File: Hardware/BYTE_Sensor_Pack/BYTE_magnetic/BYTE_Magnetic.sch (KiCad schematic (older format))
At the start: 18 parts, among them J1 PCB, M1 Motor_DC, U1 SI7210-B-11-IM2, U2 DRV2605YZFR, U3 Si7217-B-01-IV, U4 SI7210-B-12-IM2, U5 SI7210-B-13-IM2, U6 SI7210-B-14-IM2

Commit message: update sch magnetic
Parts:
- gave numbers to parts that had none: 4
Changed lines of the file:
@@
 	3385 3925 3385 3990
 $Comp
-L power:+3.3V #PWR?
+L power:+3.3V #PWR0122
 U 1 1 613FDA44
 P 3385 3685
-F 0 "#PWR?" H 3385 3535 50  0001 C CNN
+F 0 "#PWR0122" H 3385 3535 50  0001 C CNN
 F 1 "+3.3V" H 3400 3858 50  0000 C CNN
 F 2 "" H 3385 3685 50  0001 C CNN
@@
 $EndComp
 $Comp
-L Device:C_Small C?
+L Device:C_Small C2
 U 1 1 613FDA4E
 P 3385 3825
-F 0 "C?" H 3477 3871 50  0000 L CNN
+F 0 "C2" H 3477 3871 50  0000 L CNN
 F 1 "0.1uF" H 3477 3780 50  0000 L CNN
 F 2 "Capacitor_SMD:C_0603_1608Metric" H 3385 3825 50  0001 C CNN
@@
 $EndComp
 $Comp
-L power:GND #PWR?
+L power:GND #PWR0123
 U 1 1 613FDA58
 P 3385 3990
-F 0 "#PWR?" H 3385 3740 50  0001 C CNN
+F 0 "#PWR0123" H 3385 3740 50  0001 C CNN
 F 1 "GND" H 3390 3817 50  0000 C CNN
 F 2 "" H 3385 3990 50  0001 C CNN
@@
 	5150 3925 5150 3990
 $Comp
-L power:+3.3V #PWR?
+L power:+3.3V #PWR0124
 U 1 1 6140C4E9
 P 5150 3685
-F 0 "#PWR?" H 5150 3535 50  0001 C CNN
+F 0 "#PWR0124" H 5150 3535 50  0001 C CNN
 F 1 "+3.3V" H 5165 3858 50  0000 C CNN
 F 2 "" H 5150 3685 50  0001 C CNN
@@
 $EndComp
 $Comp
-L Device:C_Small C?
+L Device:C_Small C3
 U 1 1 6140C4F3
 P 5150 3825
-F 0 "C?" H 5242 3871 50  0000 L CNN
+F 0 "C3" H 5242 3871 50  0000 L CNN
 F 1 "0.1uF" H 5242 3780 50  0000 L CNN
 F 2 "Capacitor_SMD:C_0603_1608Metric" H 5150 3825 50  0001 C CNN
@@
 $EndComp
 $Comp
-L power:GND #PWR?
+L power:GND #PWR0125
 U 1 1 6140C4FD
 P 5150 3990
-F 0 "#PWR?" H 5150 3740 50  0001 C CNN
+F 0 "#PWR0125" H 5150 3740 50  0001 C CNN
 F 1 "GND" H 5155 3817 50  0000 C CNN
 F 2 "" H 5150 3990 50  0001 C CNN
@@
 	7130 3870 7130 3935
 $Comp
-L power:+3.3V #PWR?
+L power:+3.3V #PWR0126
 U 1 1 614205AE
 P 7130 3630
-F 0 "#PWR?" H 7130 3480 50  0001 C CNN
+F 0 "#PWR0126" H 7130 3480 50  0001 C CNN
 F 1 "+3.3V" H 7145 3803 50  0000 C CNN
 F 2 "" H 7130 3630 50  0001 C CNN
@@
 $EndComp
 $Comp
-L Device:C_Small C?
+L Device:C_Small C6
 U 1 1 614205B8
 P 7130 3770
-F 0 "C?" H 7222 3816 50  0000 L CNN
+F 0 "C6" H 7222 3816 50  0000 L CNN
 F 1 "0.1uF" H 7222 3725 50  0000 L CNN
 F 2 "Capacitor_SMD:C_0603_1608Metric" H 7130 3770 50  0001 C CNN
@@
 $EndComp
 $Comp
-L power:GND #PWR?
+L power:GND #PWR0127
 U 1 1 614205C2
 P 7130 3935
-F 0 "#PWR?" H 7130 3685 50  0001 C CNN
+F 0 "#PWR0127" H 7130 3685 50  0001 C CNN
 F 1 "GND" H 7135 3762 50  0000 C CNN
 F 2 "" H 7130 3935 50  0001 C CNN
@@
 	8955 3925 8955 3990
 $Comp
-L power:+3.3V #PWR?
+L power:+3.3V #PWR0128
 U 1 1 61428F42
 P 8955 3685
-F 0 "#PWR?" H 8955 3535 50  0001 C CNN
+F 0 "#PWR0128" H 8955 3535 50  0001 C CNN
 F 1 "+3.3V" H 8970 3858 50  0000 C CNN
 F 2 "" H 8955 3685 50  0001 C CNN
@@
 $EndComp
 $Comp
-L Device:C_Small C?
+L Device:C_Small C7
 U 1 1 61428F4C
 P 8955 3825
-F 0 "C?" H 9047 3871 50  0000 L CNN
+F 0 "C7" H 9047 3871 50  0000 L CNN
 F 1 "0.1uF" H 9047 3780 50  0000 L CNN
 F 2 "Capacitor_SMD:C_0603_1608Metric" H 8955 3825 50  0001 C CNN
@@
 $EndComp
 $Comp
-L power:GND #PWR?
+L power:GND #PWR0129
 U 1 1 61428F56
 P 8955 3990
-F 0 "#PWR?" H 8955 3740 50  0001 C CNN
+F 0 "#PWR0129" H 8955 3740 50  0001 C CNN
 F 1 "GND" H 8960 3817 50  0000 C CNN
 F 2 "" H 8955 3990 50  0001 C CNN

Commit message: update magnetic layout
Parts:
- removed C1, C2: 0.1uF, Capacitor_SMD:C_0603_1608Metric, symbol Device:C_Small
- removed J1: PCB, BYTE_Sensors:Magnetic_PCB, symbol Connector_Generic:Conn_01x06
- removed R3: 2.2K, Resistor_SMD:R_0603_1608Metric, symbol Device:R_Small
- removed U1: SI7210-B-11-IM2, BYTE_Sensors:SON40P140X160X40-8N-D, symbol magnetic_sensor:SI7210-B-10-IM2
- removed U2: DRV2605YZFR, BYTE_Sensors:BGA9C50P3X3_144X144X62, symbol BYTE_Magnetic-rescue:DRV2605YZFR-capacitive_sensor
- removed U3: Si7217-B-01-IV, BYTE_Sensors:SOT95P275X125-5N, symbol magnetic_sensor:Si7217-B-01-IV
- added J1: Input, BYTE_Sensors:Flex_Connector, symbol Connector_Generic:Conn_01x05
- added U1: DRV2605LDGS, Package_SO:VSSOP-10_3x3mm_P0.5mm, symbol Driver_Haptic:DRV2605LDGS
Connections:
- net labels removed: ADD0, ADD1, INT, OUT2, REG, SLEEP
- wire segments 63 -> 53
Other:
- note removed: "ADDR = 0x30"
- note removed: "Low(Open-drain)"
- moved on the sheet: C4, M1

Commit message: update magnetic sensor, merge with FSR
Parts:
- added C1: 1uF, Capacitor_SMD:C_0603_1608Metric, symbol Device:C_Small
- added J2: FSR, BYTE_Sensors:FSR_13mm, symbol Connector_Generic:Conn_01x04
- added R3, R4, R5, R6: 10K, Resistor_SMD:R_0603_1608Metric, symbol Device:R_Small
- added U2: ADS1115IDGS, Package_SO:TSSOP-10_3x3mm_P0.5mm, symbol Analog_ADC:ADS1115IDGS
- M1: footprint (none) -> BYTE_Sensors:VLV041235L
- U4, U5, U6: symbol magnetic_sensor:SI7210-B-10-IM2 -> BYTE_Magnetic-rescue:SI7210-B-10-IM2-magnetic_sensor
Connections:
- net labels added: A0, A1, A2, A3
- wire segments 53 -> 81
- no-connect marks 3 -> 1

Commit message: update pcbs
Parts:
- removed R1, R2: 2.2K, Resistor_SMD:R_0603_1608Metric, symbol Device:R_Small
- removed R3, R4, R5, R6: 10K, Resistor_SMD:R_0603_1608Metric, symbol Device:R_Small
- added RN1: R_Pack04, Resistor_SMD:R_Array_Convex_4x0603, symbol Device:R_Pack04
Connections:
- net A0: now also RN1.3 (R3.1)
- net A1: now also RN1.4 (R4.1)
- net A2: now also RN1.1 (R1.1)
- net A3: now also RN1.2 (R2.1)
- net GND: now also RN1.5 (R4.2), RN1.6 (R3.2), RN1.7 (R2.2), RN1.8 (R1.2)
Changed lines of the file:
@@
 Comment4 ""
 $EndDescr
-Text Label 2020 1260 0    50   ~ 0
-SCL
-Text Label 2020 1360 0    50   ~ 0
-SDA
-$Comp
-L power:+3.3V #PWR0107
-U 1 1 6139A81A
-P 2450 980
-F 0 "#PWR0107" H 2450 830 50  0001 C CNN
-F 1 "+3.3V" H 2465 1153 50  0000 C CNN
-F 2 "" H 2450 980 50  0001 C CNN
-F 3 "" H 2450 980 50  0001 C CNN
-	1    2450 980
-	1    0    0    -1
-$EndComp
-$Comp
-L power:+3.3V #PWR0108
-U 1 1 6139B3E0
-P 2725 975
-F 0 "#PWR0108" H 2725 825 50  0001 C CNN
-F 1 "+3.3V" H 2740 1148 50  0000 C CNN
-F 2 "" H 2725 975 50  0001 C CNN
-F 3 "" H 2725 975 50  0001 C CNN
-	1    2725 975
-	1    0    0    -1
-$EndComp
-$Comp
-L Device:R_Small R1
-U 1 1 6139B985
-P 2450 1115
-F 0 "R1" H 2315 1155 50  0000 L CNN
-F 1 "2.2K" H 2245 1070 50  0000 L CNN
-F 2 "Resistor_SMD:R_0603_1608Metric" H 2450 1115 50  0001 C CNN
-F 3 "~" H 2450 1115 50  0001 C CNN
-	1    2450 1115
-	1    0    0    -1
-$EndComp
-Wire Wire Line
-	2725 975  2725 1015
-Wire Wire Line
-	2450 980  2450 1015
-Wire Wire Line
-	2450 1260 2450 1215
-Wire Wire Line
-	2020 1260 2450 1260
-Wire Wire Line
-	2020 1360 2725 1360
-Wire Wire Line
-	2725 1215 2725 1360
-$Comp
-L Device:R_Small R2
-U 1 1 6139C2A7
-P 2725 1115
-F 0 "R2" H 2590 1150 50  0000 L CNN
-F 1 "2.2K" H 2515 1080 50  0000 L CNN
-F 2 "Resistor_SMD:R_0603_1608Metric" H 2725 1115 50  0001 C CNN
-F 3 "~" H 2725 1115 50  0001 C CNN
-	1    2725 1115
-	1    0    0    -1
-$EndComp
 Wire Wire Line
 	9475 1420 9985 1420
@@
 $EndComp
 $Comp
-L Device:R_Small R3
-U 1 1 6146D0E5
-P 4305 2635
-F 0 "R3" V 4300 2585 50  0000 L CNN
-F 1 "10K" V 4300 2195 50  0000 L CNN
-F 2 "Resistor_SMD:R_0603_1608Metric" H 4305 2635 50  0001 C CNN
-F 3 "~" H 4305 2635 50  0001 C CNN
-	1    4305 2635
+L Device:R_Pack04 RN1
+U 1 1 61491CB7
+P 4150 2600
+F 0 "RN1" H 4338 2646 50  0000 L CNN
+F 1 "R_Pack04" H 4338 2555 50  0000 L CNN
+F 2 "Resistor_SMD:R_Array_Convex_4x0603" V 4425 2600 50  0001 C CNN
+F 3 "~" H 4150 2600 50  0001 C CNN
+	1    4150 2600
 	-1   0    0    1
 $EndComp
-Text Label 4005 2355 3    50   ~ 0
+Wire Wire Line
+	4050 2800 4150 2800
+Wire Wire Line
+	4150 2800 4250 2800
+Connection ~ 4150 2800
+Wire Wire Line
+	4250 2800 4350 2800
+Connection ~ 4250 2800
+$Comp
+L power:GND #PWR0107
+U 1 1 614A2797
+P 4350 2850
+F 0 "#PWR0107" H 4350 2600 50  0001 C CNN
+F 1 "GND" H 4355 2677 50  0000 C CNN
+F 2 "" H 4350 2850 50  0001 C CNN
+F 3 "" H 4350 2850 50  0001 C CNN
+	1    4350 2850
+	1    0    0    -1
+$EndComp
+Wire Wire Line
+	4350 2850 4350 2800
+Connection ~ 4350 2800
+Wire Wire Line
+	4050 2250 4050 2400
+Wire Wire Line
+	4150 2400 4150 2250
+Wire Wire Line
+	4250 2400 4250 2250
+Wire Wire Line
+	4350 2400 4350 2250
+Text Label 4050 2250 3    50   ~ 0
+A1
+Text Label 4150 2250 3    50   ~ 0
 A0
-Wire Wire Line
-	4005 2355 4005 2535
-Text Label 4105 2355 3    50   ~ 0
-A1
-Wire Wire Line
-	4105 2355 4105 2535
-Text Label 4205 2355 3    50   ~ 0
+Text Label 4350 2250 3    50   ~ 0
 A2
-Wire Wire Line
-	4205 2355 4205 2535
-Text Label 4305 2355 3    50   ~ 0
+Text Label 4250 2250 3    50   ~ 0
 A3
-Wire Wire Line
-	4305 2355 4305 2535
-$Comp
-L Device:R_Small R4
-U 1 1 61479B09
-P 4205 2635
-F 0 "R4" V 4200 2580 50  0000 L CNN
-F 1 "10K" V 4205 2195 50  0000 L CNN
-F 2 "Resistor_SMD:R_0603_1608Metric" H 4205 2635 50  0001 C CNN
-F 3 "~" H 4205 2635 50  0001 C CNN
-	1    4205 2635
-	-1   0    0    1
-$EndComp
-$Comp
-L Device:R_Small R5
-U 1 1 6147E339
-P 4105 2635
-F 0 "R5" V 4100 2580 50  0000 L CNN
-F 1 "10K" V 4105 2200 50  0000 L CNN
-F 2 "Resistor_SMD:R_0603_1608Metric" H 4105 2635 50  0001 C CNN
-F 3 "~" H 4105 2635 50  0001 C CNN
-	1    4105 2635
-	-1   0    0    1
-$EndComp
-$Comp
-L Device:R_Small R6
-U 1 1 6147E7F5
-P 4005 2635
-F 0 "R6" V 4000 2580 50  0000 L CNN
-F 1 "10K" V 4005 2200 50  0000 L CNN
-F 2 "Resistor_SMD:R_0603_1608Metric" H 4005 2635 50  0001 C CNN
-F 3 "~" H 4005 2635 50  0001 C CNN
-	1    4005 2635
-	-1   0    0    1
-$EndComp
-Wire Wire Line
-	4005 2735 4005 2805
-Wire Wire Line
-	4005 2805 4105 2805
-Connection ~ 4305 2805
-Wire Wire Line
-	4305 2805 4305 2735
-Wire Wire Line
-	4205 2735 4205 2805
-Connection ~ 4205 2805
-Wire Wire Line
-	4205 2805 4305 2805
-Wire Wire Line
-	4105 2735 4105 2805
-Connection ~ 4105 2805
-Wire Wire Line
-	4105 2805 4205 2805
-$Comp
-L power:GND #PWR0118
-U 1 1 61495E33
-P 4305 2885
-F 0 "#PWR0118" H 4305 2635 50  0001 C CNN
-F 1 "GND" H 4310 2712 50  0000 C CNN
-F 2 "" H 4305 2885 50  0001 C CNN
-F 3 "" H 4305 2885 50  0001 C CNN
-	1    4305 2885
-	1    0    0    -1
-$EndComp
-Wire Wire Line
-	4305 2805 4305 2885
 $EndSCHEMATC

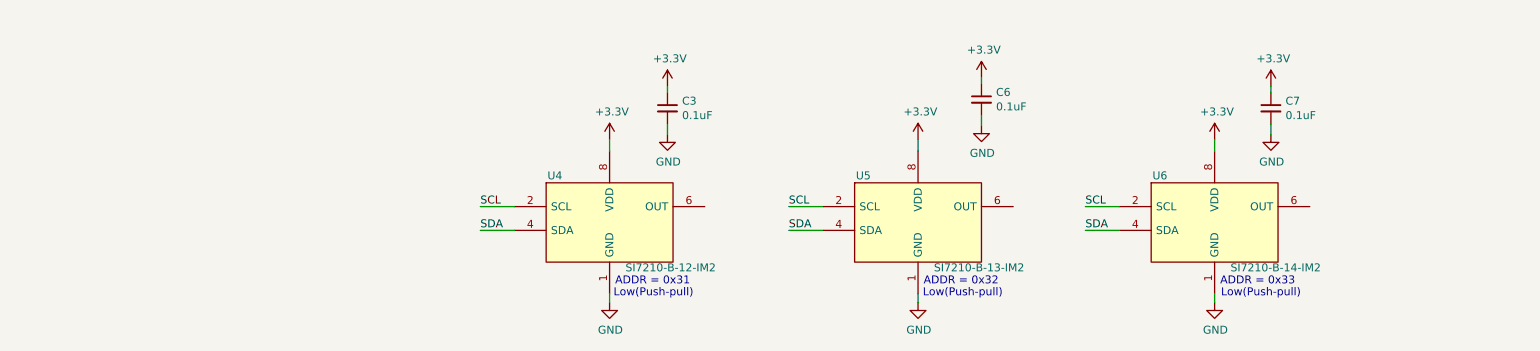
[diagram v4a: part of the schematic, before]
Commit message: update magentic adding I2C I/O controller
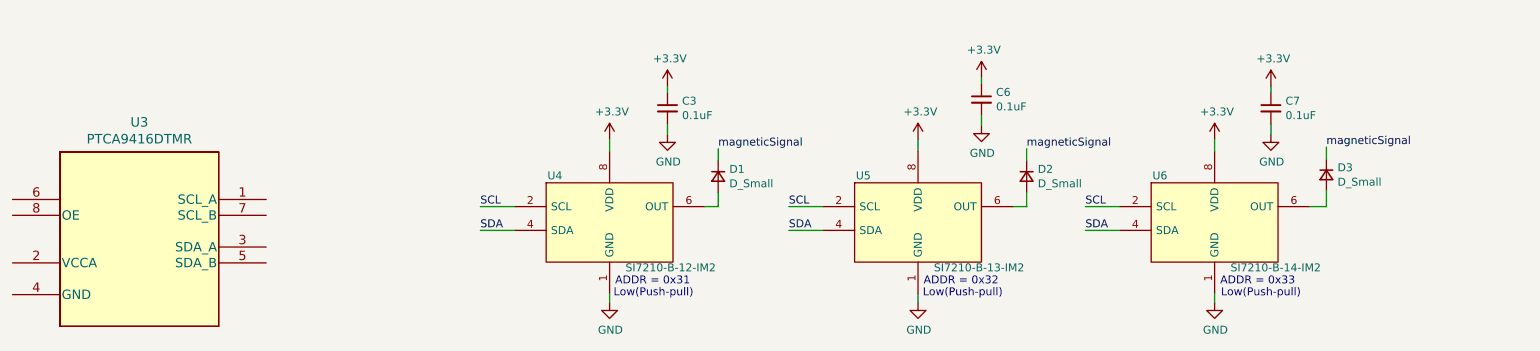
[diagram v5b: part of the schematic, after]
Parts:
- added D1, D2, D3: D_Small, Diode_SMD:D_0603_1608Metric, symbol Device:D_Small
- added U3: PTCA9416DTMR, BYTE_Sensors:PTCA9416DTMR, symbol magnetic_sensor:PTCA9416DTMR
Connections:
- net at U4.6 (OUT): now also D1.2 (A)
- net at U5.6 (OUT): now also D2.2 (A)
- net at U6.6 (OUT): now also D3.2 (A)
- new net magneticSignal: D1.1 (K), D2.1 (K), D3.1 (K)
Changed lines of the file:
@@
 Text Label 4250 2250 3    50   ~ 0
 A3
+$Comp
+L Device:D_Small D1
+U 1 1 614CCBCC
+P 5470 4255
+F 0 "D1" V 5424 4325 50  0000 L CNN
+F 1 "D_Small" V 5515 4325 50  0000 L CNN
+F 2 "Diode_SMD:D_0603_1608Metric" V 5470 4255 50  0001 C CNN
+F 3 "~" V 5470 4255 50  0001 C CNN
+	1    5470 4255
+	0    1    1    0
+$EndComp
+Wire Wire Line
+	5470 4355 5470 4445
+Wire Wire Line
+	5470 4445 5385 4445
+$Comp
+L Device:D_Small D2
+U 1 1 614D0F0E
+P 7415 4255
+F 0 "D2" V 7369 4325 50  0000 L CNN
+F 1 "D_Small" V 7460 4325 50  0000 L CNN
+F 2 "Diode_SMD:D_0603_1608Metric" V 7415 4255 50  0001 C CNN
+F 3 "~" V 7415 4255 50  0001 C CNN
+	1    7415 4255
+	0    1    1    0
+$EndComp
+Wire Wire Line
+	7415 4355 7415 4445
+Wire Wire Line
+	7415 4445 7330 4445
+$Comp
+L Device:D_Small D3
+U 1 1 614D3973
+P 9305 4245
+F 0 "D3" V 9259 4315 50  0000 L CNN
+F 1 "D_Small" V 9350 4315 50  0000 L CNN
+F 2 "Diode_SMD:D_0603_1608Metric" V 9305 4245 50  0001 C CNN
+F 3 "~" V 9305 4245 50  0001 C CNN
+	1    9305 4245
+	0    1    1    0
+$EndComp
+Wire Wire Line
+	9305 4345 9305 4445
+Wire Wire Line
+	9305 4445 9200 4445
+Text Label 9305 4070 0    50   ~ 0
+magneticSignal
+Wire Wire Line
+	9305 4070 9305 4145
+Text Label 7415 4080 0    50   ~ 0
+magneticSignal
+Wire Wire Line
+	7415 4080 7415 4155
+Text Label 5470 4080 0    50   ~ 0
+magneticSignal
+Wire Wire Line
+	5470 4080 5470 4155
+$Comp
+L magnetic_sensor:PTCA9416DTMR U3
+U 1 1 614EB528
+P 1020 4400
+F 0 "U3" H 1820 4887 60  0000 C CNN
+F 1 "PTCA9416DTMR" H 1820 4781 60  0000 C CNN
+F 2 "BYTE_Sensors:PTCA9416DTMR" H 1820 4740 60  0001 C CNN
+F 3 "" H 1020 4400 60  0000 C CNN
+	1    1020 4400
+	1    0    0    -1
+$EndComp
 $EndSCHEMATC

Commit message: update magnetic sensor
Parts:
- removed U3: PTCA9416DTMR, BYTE_Sensors:PTCA9416DTMR, symbol magnetic_sensor:PTCA9416DTMR
- added U3: PTCA9536BDTMR, BYTE_Sensors:PTCA9416DTMR, symbol magnetic_sensor:PTCA9536BDTMR
- J2: footprint BYTE_Sensors:FSR_13mm -> (none)
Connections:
- net +3V3: now also J1.3 (Pin_3), U3.7 (VCC); no longer J1.5 (Pin_5)
- net GND: now also J1.5 (Pin_5), U1.4 (IN/TRIG), U3.3 (GND); no longer J1.1 (Pin_1), RN1.5 (R4.2), RN1.6 (R3.2), RN1.7 (R2.2), RN1.8 (R1.2)
- net SCL: now also J1.2 (Pin_2), U3.5 (SCL); no longer J1.3 (Pin_3)
- net SDA: now also J1.1 (Pin_1), U3.6 (SDA); no longer J1.2 (Pin_2)
- net magneticSignal: now also U3.8 (P1)
- net ALERT: now reaches U2.2 (ALERT/RDY)
- net ALERT: now also U3.2 (P2)
- net IN_TRIG renamed INT_OUT
- net INT_OUT: now also U3.4 (P3/INT); no longer U1.4 (IN/TRIG)
- new net FSR_CTRL: RN1.5 (R4.2), RN1.6 (R3.2), RN1.7 (R2.2), RN1.8 (R1.2), U3.1 (P0)
- no-connect marks 1 -> 0
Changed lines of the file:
@@
 Text Label 7855 1835 0    50   ~ 0
 SDA
-Text Label 7855 2135 0    50   ~ 0
-IN_TRIG
-Wire Wire Line
-	7855 2135 8120 2135
 Wire Wire Line
 	7855 2235 8120 2235
@@
 L power:+3.3V #PWR0101
 U 1 1 613F1152
-P 1810 1955
-F 0 "#PWR0101" H 1810 1805 50  0001 C CNN
-F 1 "+3.3V" H 1825 2128 50  0000 C CNN
-F 2 "" H 1810 1955 50  0001 C CNN
-F 3 "" H 1810 1955 50  0001 C CNN
-	1    1810 1955
-	1    0    0    -1
-$EndComp
-Wire Wire Line
-	1810 1955 1810 2055
-Wire Wire Line
-	1810 2055 1645 2055
+P 1965 1920
+F 0 "#PWR0101" H 1965 1770 50  0001 C CNN
+F 1 "+3.3V" H 1980 2093 50  0000 C CNN
+F 2 "" H 1965 1920 50  0001 C CNN
+F 3 "" H 1965 1920 50  0001 C CNN
+	1    1965 1920
+	1    0    0    -1
+$EndComp
 $Comp
 L power:GND #PWR0109
 U 1 1 613F34F1
-P 1815 2580
-F 0 "#PWR0109" H 1815 2330 50  0001 C CNN
-F 1 "GND" H 1820 2407 50  0000 C CNN
-F 2 "" H 1815 2580 50  0001 C CNN
-F 3 "" H 1815 2580 50  0001 C CNN
-	1    1815 2580
-	1    0    0    -1
-$EndComp
-Wire Wire Line
-	1815 2580 1815 2455
-Wire Wire Line
-	1815 2455 1645 2455
-Text Label 1910 2155 2    50   ~ 0
-IN_TRIG
+P 2150 2195
+F 0 "#PWR0109" H 2150 1945 50  0001 C CNN
+F 1 "GND" H 2155 2022 50  0000 C CNN
+F 2 "" H 2150 2195 50  0001 C CNN
+F 3 "" H 2150 2195 50  0001 C CNN
+	1    2150 2195
+	1    0    0    -1
+$EndComp
 Wire Wire Line
 	1910 2155 1645 2155
-Text Label 1910 2255 2    50   ~ 0
+Text Label 1910 2355 2    50   ~ 0
 SCL
 Wire Wire Line
-	1910 2255 1645 2255
-Text Label 1910 2355 2    50   ~ 0
+	1910 2355 1645 2355
+Text Label 1910 2455 2    50   ~ 0
 SDA
 Wire Wire Line
-	1910 2355 1645 2355
+	1910 2455 1645 2455
 Wire Wire Line
 	9985 1420 9985 1585
@@
 	1    0    0    -1
 $EndComp
-NoConn ~ 5785 1815
 Text Label 6050 2115 2    50   ~ 0
 SDA
@@
 F 0 "J2" H 3153 1655 50  0000 C CNN
 F 1 "FSR" H 3153 1746 50  0000 C CNN
-F 2 "BYTE_Sensors:FSR_13mm" H 3235 2080 50  0001 C CNN
+F 2 "" H 3235 2080 50  0001 C CNN
 F 3 "~" H 3235 2080 50  0001 C CNN
 	1    3235 2080
@@
 	4250 2800 4350 2800
 Connection ~ 4250 2800
-$Comp
-L power:GND #PWR0107
-U 1 1 614A2797
-P 4350 2850
-F 0 "#PWR0107" H 4350 2600 50  0001 C CNN
-F 1 "GND" H 4355 2677 50  0000 C CNN
-F 2 "" H 4350 2850 50  0001 C CNN
-F 3 "" H 4350 2850 50  0001 C CNN
-	1    4350 2850
-	1    0    0    -1
-$EndComp
-Wire Wire Line
-	4350 2850 4350 2800
 Connection ~ 4350 2800
 Wire Wire Line
@@
 Wire Wire Line
 	5470 4080 5470 4155
-$Comp
-L magnetic_sensor:PTCA9416DTMR U3
-U 1 1 614EB528
-P 1020 4400
-F 0 "U3" H 1820 4887 60  0000 C CNN
-F 1 "PTCA9416DTMR" H 1820 4781 60  0000 C CNN
-F 2 "BYTE_Sensors:PTCA9416DTMR" H 1820 4740 60  0001 C CNN
-F 3 "" H 1020 4400 60  0000 C CNN
-	1    1020 4400
-	1    0    0    -1
-$EndComp
+Wire Wire Line
+	1645 2255 1965 2255
+Wire Wire Line
+	1965 1920 1965 2255
+Wire Wire Line
+	2150 2055 1645 2055
+Wire Wire Line
+	2150 2055 2150 2195
+$Comp
+L magnetic_sensor:PTCA9536BDTMR U3
+U 1 1 61509300
+P 1500 4415
+F 0 "U3" H 2225 5068 60  0000 C CNN
+F 1 "PTCA9536BDTMR" H 2765 3995 60  0000 C CNN
+F 2 "BYTE_Sensors:PTCA9416DTMR" H 2300 4755 60  0001 C CNN
+F 3 "https://www.ti.com/lit/ds/symlink/tca9536.pdf?ts=1632417802890&ref_url=https%253A%252F%252Fwww.ti.com%252Fproduct%252FTCA9536" H 2300 5112 60  0001 C CNN
+	1    1500 4415
+	1    0    0    -1
+$EndComp
+$Comp
+L power:+3.3V #PWR0108
+U 1 1 61514F71
+P 2350 3830
+F 0 "#PWR0108" H 2350 3680 50  0001 C CNN
+F 1 "+3.3V" H 2365 4003 50  0000 C CNN
+F 2 "" H 2350 3830 50  0001 C CNN
+F 3 "" H 2350 3830 50  0001 C CNN
+	1    2350 3830
+	1    0    0    -1
+$EndComp
+Wire Wire Line
+	2350 3830 2350 3965
+$Comp
+L power:GND #PWR0118
+U 1 1 615183EC
+P 2350 5015
+F 0 "#PWR0118" H 2350 4765 50  0001 C CNN
+F 1 "GND" H 2355 4842 50  0000 C CNN
+F 2 "" H 2350 5015 50  0001 C CNN
+F 3 "" H 2350 5015 50  0001 C CNN
+	1    2350 5015
+	1    0    0    -1
+$EndComp
+Wire Wire Line
+	2350 4965 2350 5015
+Wire Wire Line
+	6050 1815 5785 1815
+Text Label 6050 1815 2    50   ~ 0
+ALERT
+Text Label 1455 4665 0    50   ~ 0
+INT_OUT
+Wire Wire Line
+	1455 4665 1700 4665
+Text Label 1910 2155 2    50   ~ 0
+INT_OUT
+Text Label 1485 4465 0    50   ~ 0
+SCL
+Wire Wire Line
+	1485 4465 1700 4465
+Text Label 1485 4365 0    50   ~ 0
+SDA
+Wire Wire Line
+	1485 4365 1700 4365
+Text Label 4350 2940 2    50   ~ 0
+FSR_CTRL
+Wire Wire Line
+	4350 2800 4350 2940
+$Comp
+L power:GND #PWR0107
+U 1 1 615E5E49
+P 7725 2225
+F 0 "#PWR0107" H 7725 1975 50  0001 C CNN
+F 1 "GND" H 7730 2052 50  0000 C CNN
+F 2 "" H 7725 2225 50  0001 C CNN
+F 3 "" H 7725 2225 50  0001 C CNN
+	1    7725 2225
+	1    0    0    -1
+$EndComp
+Wire Wire Line
+	7725 2225 7725 2135
+Wire Wire Line
+	7725 2135 8120 2135
+Text Label 3055 4365 2    50   ~ 0
+FSR_CTRL
+Wire Wire Line
+	3055 4365 2750 4365
+Wire Wire Line
+	2750 4465 3295 4465
+Text Label 3295 4465 2    50   ~ 0
+magneticSignal
+Wire Wire Line
+	3015 4565 2750 4565
+Text Label 3015 4565 2    50   ~ 0
+ALERT
 $EndSCHEMATC
